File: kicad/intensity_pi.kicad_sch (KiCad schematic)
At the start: 67 parts, among them J1 Input A, J2 Input B / Setpoint, J3 Monitor, J4 Output, J7 select 1, SW1 SW_SPDT, SW2 SW_SPDT, SW3 SW_SPDT, SW5 EG6100-ND, U1 LM4040DBZ-5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

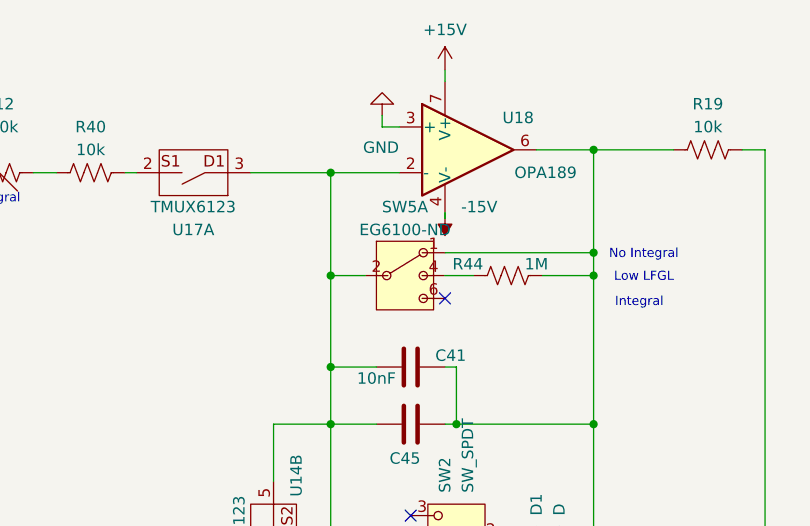
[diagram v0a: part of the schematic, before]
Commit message: Rearranged Edge Componenets, simpler board, wider but shorter depth
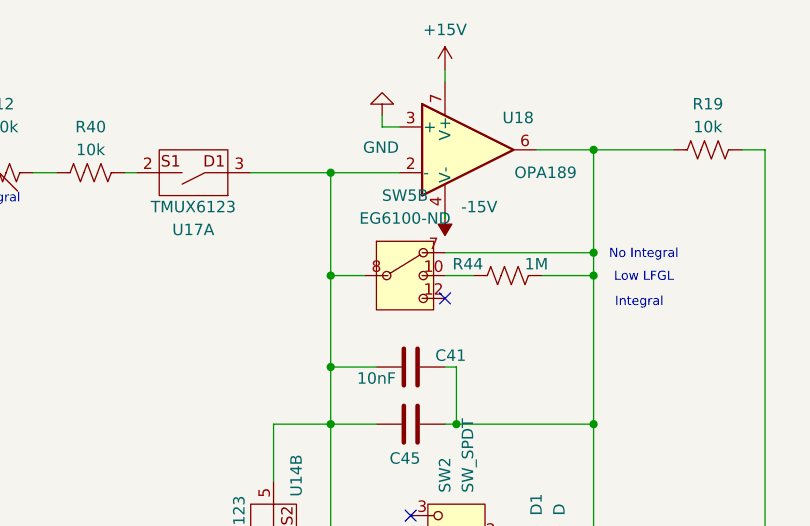
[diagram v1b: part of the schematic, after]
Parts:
- removed SW5: EG6100-ND, Custom_Footprints:Right Angle 3PDT Switch, symbol Custom_Symbols:DP3T_1
- added SW5: EG6100-ND, Custom_Footprints:Right Angle 3PDT Switch, symbol Custom_Symbols:DP3T_1
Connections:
- net at C41.1, C45.2, D1.2 (A)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: now also SW5.7
- net at C41.2, C45.1, SW2.1 (A)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: now also SW5.8
- net at R44.1: now also SW5.10
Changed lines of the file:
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@@
+	)
+	(symbol
+		(lib_id "Custom_Symbols:DP3T_1")
+		(at 179.07 41.91 0)
+		(unit 2)
+		(exclude_from_sim no)
+		(in_bom yes)
+		(on_board yes)
+		(dnp no)
+		(fields_autoplaced yes)
+		(property "Reference" "SW5"
+			(at 179.705 33.02 0)
+			(effects
+				(font
+					(size 1.27 1.27)
+				)
+			)
+		)
+		(property "Value" "EG6100-ND"
+			(at 179.705 35.56 0)
+			(effects
+				(font
+					(size 1.27 1.27)
+				)
+			)
+		)
+		(property "Footprint" "Custom_Footprints:Right Angle 3PDT Switch"
+			(at 179.07 41.91 0)
+			(effects
+				(font
+					(size 1.27 1.27)
+				)
+				(hide yes)
+			)
+		)
+		(property "Datasheet" ""
+			(at 179.07 41.91 0)
+			(effects
+				(font
+					(size 1.27 1.27)
+				)
+				(hide yes)
+			)
+		)
+		(property "Description" ""
+			(at 179.07 41.91 0)
+			(effects
+				(font
+					(size 1.27 1.27)
+				)
+				(hide yes)
+			)
+		)
+		(property "DIGIKEY" "EG6100-ND"
+			(at 179.07 41.91 0)
+			(effects
+				(font
+					(size 1.27 1.27)
+				)
+				(hide yes)
+			)
+		)
+		(property "PARTNO" "1004P6T1B4M7RE"
+			(at 179.07 41.91 0)
+			(effects
+				(font
+					(size 1.27 1.27)
+				)
+				(hide yes)
+			)
+		)
+		(property "MPN" ""
+			(at 179.07 41.91 0)
+			(effects
+				(font
+					(size 1.27 1.27)
+				)
+				(hide yes)
+			)
+		)
+		(pin "9"
+		)
+		(pin "10"
+		)
+		(pin "3"
+		)
+		(pin "5"
+		)
+		(pin "12"
+		)
+		(pin "8"
+		)
+		(pin "11"
+		)
+		(pin "7"
+		)
+		(pin "13"
+		)
+		(pin "6"
+		)
+		(pin "2"
+		)
+		(pin "4"
+		)
+		(pin "1"
+		)
+		(instances
+			(project "intensity_pi"
+				(path "/3a3d7bcb-6fa5-41ef-9ea1-6d4ab7c492fd"
+					(reference "SW5")
+					(unit 2)
+				)
+			)
+		)
 	)
 	(symbol
@@
 					(unit 1)
 				)
-			)
-		)
-	)
-	(symbol
-		(lib_id "Custom_Symbols:DP3T_1")
-		(at 179.07 41.91 0)
-		(unit 1)
-		(exclude_from_sim no)
-		(in_bom yes)
-		(on_board yes)
-		(dnp no)
-		(fields_autoplaced yes)
-		(property "Reference" "SW5"
-			(at 179.705 34.29 0)
-			(effects
-				(font
-					(size 1.27 1.27)
-				)
-			)
-		)
-		(property "Value" "EG6100-ND"
-			(at 179.705 36.83 0)
-			(effects
-				(font
-					(size 1.27 1.27)
-				)
-			)
-		)
-		(property "Footprint" "Custom_Footprints:Right Angle 3PDT Switch"
-			(at 179.07 41.91 0)
-			(effects
-				(font
-					(size 1.27 1.27)
-				)
-				(hide yes)
-			)
-		)
-		(property "Datasheet" ""
-			(at 179.07 41.91 0)
-			(effects
-				(font
-					(size 1.27 1.27)
-				)
-				(hide yes)
-			)
-		)
-		(property "Description" ""
-			(at 179.07 41.91 0)
-			(effects
-				(font
-					(size 1.27 1.27)
-				)
-				(hide yes)
-			)
-		)
-		(property "DIGIKEY" "EG6100-ND"
-			(at 179.07 41.91 0)
-			(effects
-				(font
-					(size 1.27 1.27)
-				)
-				(hide yes)
-			)
-		)
-		(property "PARTNO" "1004P6T1B4M7RE"
-			(at 179.07 41.91 0)
-			(effects
-				(font
-					(size 1.27 1.27)
-				)
-				(hide yes)
-			)
-		)
-		(property "MPN" ""
-			(at 179.07 41.91 0)
-			(effects
-				(font
-					(size 1.27 1.27)
-				)
-				(hide yes)
-			)
-		)
-		(pin "9"
-		)
-		(pin "10"
-		)
-		(pin "3"
-		)
-		(pin "5"
-		)
-		(pin "12"
-		)
-		(pin "8"
-		)
-		(pin "11"
-		)
-		(pin "7"
-		)
-		(pin "13"
-		)
-		(pin "6"
-		)
-		(pin "2"
-		)
-		(pin "4"
-		)
-		(pin "1"
-		)
-		(instances
-			(project "intensity_pi"
-				(path "/3a3d7bcb-6fa5-41ef-9ea1-6d4ab7c492fd"
-					(reference "SW5")
-					(unit 1)
-				)

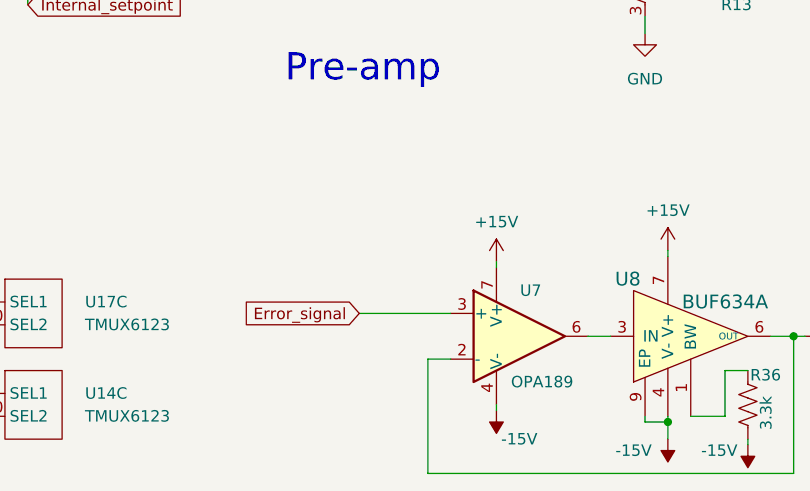
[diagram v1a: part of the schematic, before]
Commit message: Added 1k resistor to monitor, TODO: check BOM, reorg PI+LFGL, check power planes/return path, move A,B closer to PI, compress vertically
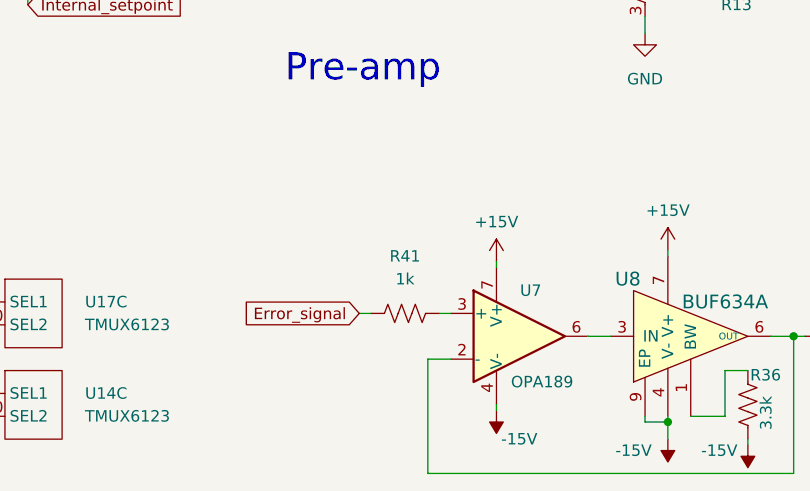
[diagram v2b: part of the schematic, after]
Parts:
- added R41: 1k, Resistor_SMD:R_0805_2012Metric, symbol Device:R_US
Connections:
- net Error_signal: now also R41.2; no longer U7.3 (+)
- new net: R41.1, U7.3 (+)
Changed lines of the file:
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@@
 	(wire
 		(pts
+			(xy 109.22 179.07) (xy 110.49 179.07)
+		)
+		(stroke
+			(width 0)
+			(type default)
+		)
+	)
+	(wire
+		(pts
 			(xy 241.935 114.3) (xy 262.89 114.3)
 		)
@@
 	(wire
 		(pts
-			(xy 109.22 179.07) (xy 119.38 179.07)
-		)
-		(stroke
-			(width 0)
-			(type default)
-		)
-	)
-	(wire
-		(pts
 			(xy 219.71 114.3) (xy 234.315 114.3)
 		)
@@
 	(wire
 		(pts
+			(xy 118.11 179.07) (xy 119.38 179.07)
+		)
+		(stroke
+			(width 0)
+			(type default)
+		)
+	)
+	(wire
+		(pts
 			(xy 25.4 67.31) (xy 25.4 69.85)
 		)
@@
 					(unit 1)
 				)
+			)
+		)
+	)
+	(symbol
+		(lib_id "Device:R_US")
+		(at 114.3 179.07 270)
+		(unit 1)
+		(exclude_from_sim no)
+		(in_bom yes)
+		(on_board yes)
+		(dnp no)
+		(fields_autoplaced yes)
+		(property "Reference" "R41"
+			(at 114.3 172.72 90)
+			(effects
+				(font
+					(size 1.27 1.27)
+				)
+			)
+		)
+		(property "Value" "1k"
+			(at 114.3 175.26 90)
+			(effects
+				(font
+					(size 1.27 1.27)
+				)
+			)
+		)
+		(property "Footprint" "Resistor_SMD:R_0805_2012Metric"
+			(at 114.046 180.086 90)
+			(effects
+				(font
+					(size 1.27 1.27)
+				)
+				(hide yes)
+			)
+		)
+		(property "Datasheet" "~"
+			(at 114.3 179.07 0)
+			(effects
+				(font
+					(size 1.27 1.27)
+				)
+				(hide yes)
+			)
+		)
+		(property "Description" ""
+			(at 114.3 179.07 0)
+			(effects
+				(font
+					(size 1.27 1.27)
+				)
+				(hide yes)
+			)
+		)
+		(property "DIGIKEY" ""
+			(at 114.3 179.07 0)
+			(effects
+				(font
+					(size 1.27 1.27)
+				)
+				(hide yes)
+			)
+		)
+		(property "MPN" ""
+			(at 114.3 179.07 0)
+			(effects
+				(font
+					(size 1.27 1.27)
+				)
+				(hide yes)
+			)
+		)
+		(pin "1"
+		)
+		(pin "2"
+		)
+		(instances
+			(project "intensity_pi"
+				(path "/3a3d7bcb-6fa5-41ef-9ea1-6d4ab7c492fd"
+					(reference "R41")
+					(unit 1)
+				)

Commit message: Minor Layout updates, replaced old component part no's, added part no's for rest of parts
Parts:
- C1, C10: DIGIKEY (none) -> 1276-6840-2-ND; PARTNO (none) -> CL21B104KCFNNNE
- C12: DIGIKEY (none) -> 399-C0805C101J5GACTUTR-ND; PARTNO (none) -> C0805C101J5GACTU
- C41: DIGIKEY (none) -> 399-C0805C103K5RACTUTR-ND; PARTNO (none) -> C0805C103K5RACTU
- R1, R10, R19, R2, R20, R22, R27, R3, R4, R40, R5, R6, R7, R8: PARTNO (none) -> RN73H2ATTD1002B25
- R12, RV8: DIGIKEY (none) -> 3590P-2-104L-ND; PARTNO (none) -> 3590P-2-104L
- R13: DIGIKEY (none) -> 118-CRT0805-BY-5001EASTR-ND; PARTNO (none) -> CRT0805-BY-5001EAS
- R14: DIGIKEY 2019-RN73H2ATTD1002B25CT-ND -> 3590S-2-103L-ND; PARTNO (none) -> 3590S-2-103L
- R15, R23: DIGIKEY (none) -> 541-CRCW080550R0FKTATR-ND; PARTNO (none) -> CRCW080550R0FKTA
- R16: DIGIKEY (none) -> P100KDATR-ND; PARTNO (none) -> ERA-6AEB104V
- R17, R21, R24, R26, R41, R9: DIGIKEY (none) -> 5831-2-2176327-5TR-ND; PARTNO (none) -> 2-2176327-5
- R33, R34: DIGIKEY 2019-RN73H2ATTD1002B25CT-ND -> (none)
- R35, R36: DIGIKEY 2019-RN73H2ATTD3301B25CT-ND -> 311-3.30KCRTR-ND; PARTNO (none) -> RC0805FR-073K3L
- R43, R46: DIGIKEY (none) -> A126334TR-ND; PARTNO (none) -> CRG0805F11K
- RV3: DIGIKEY (none) -> 3590S-2-502L-ND; PARTNO (none) -> 3590S-2-502L

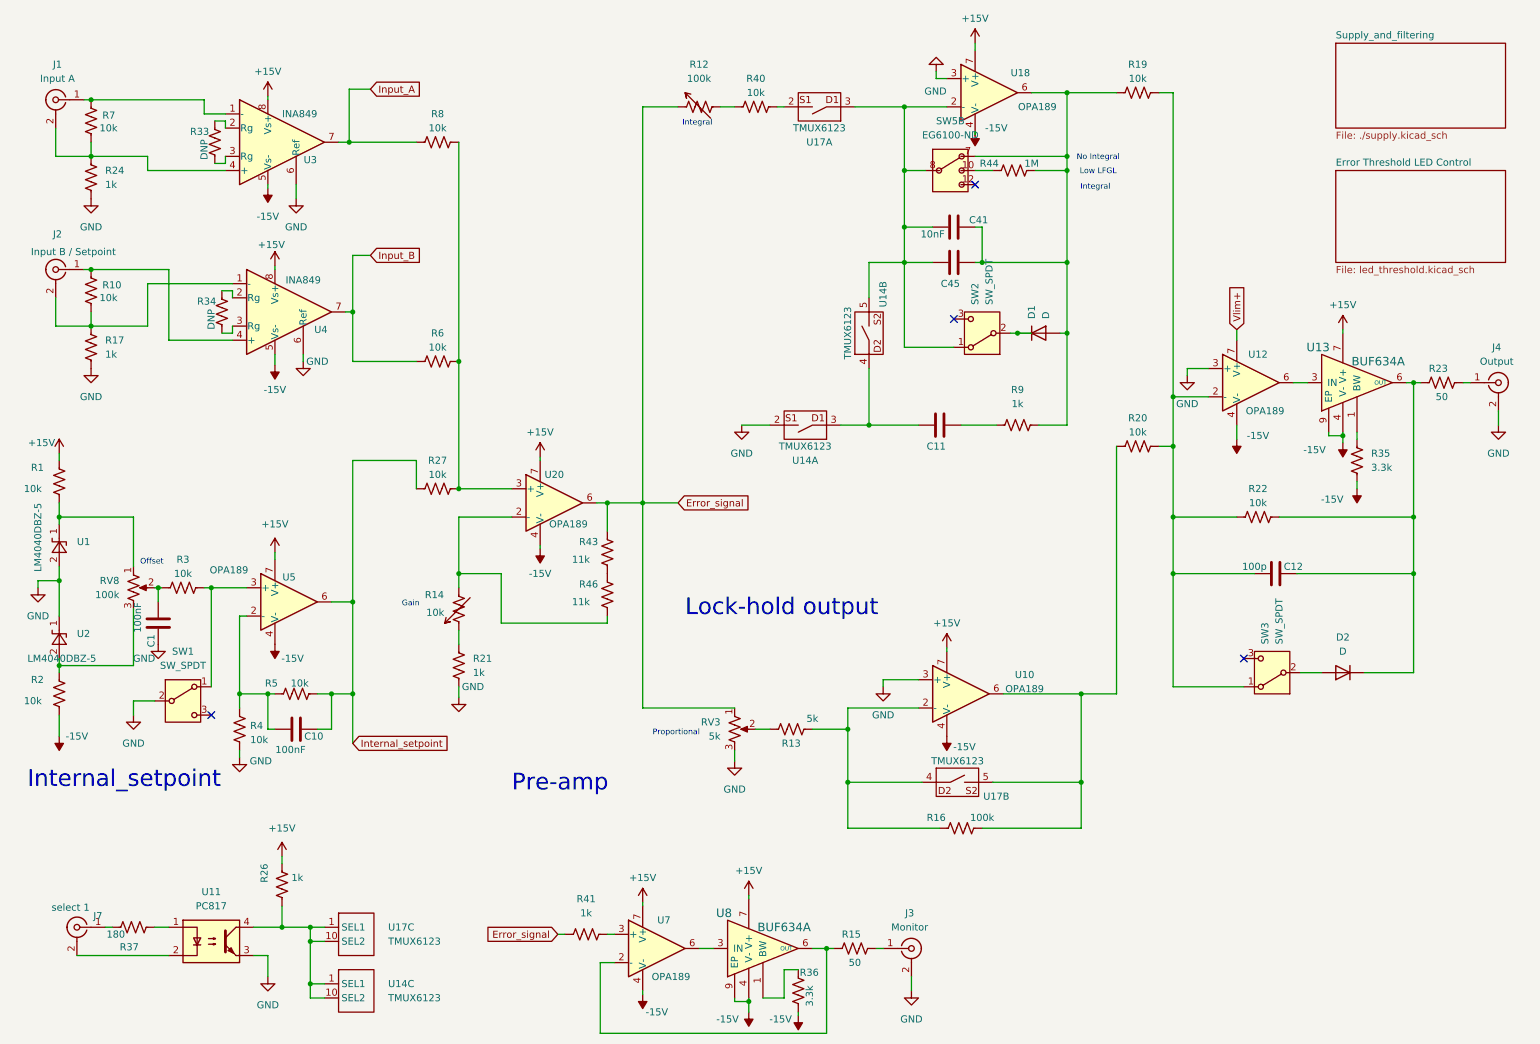
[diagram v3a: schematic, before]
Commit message: Revert change to Library Footprint for switch, update schematic to use resistance between pins 2,3 as starting at maximum, decreasing down on CW rotation
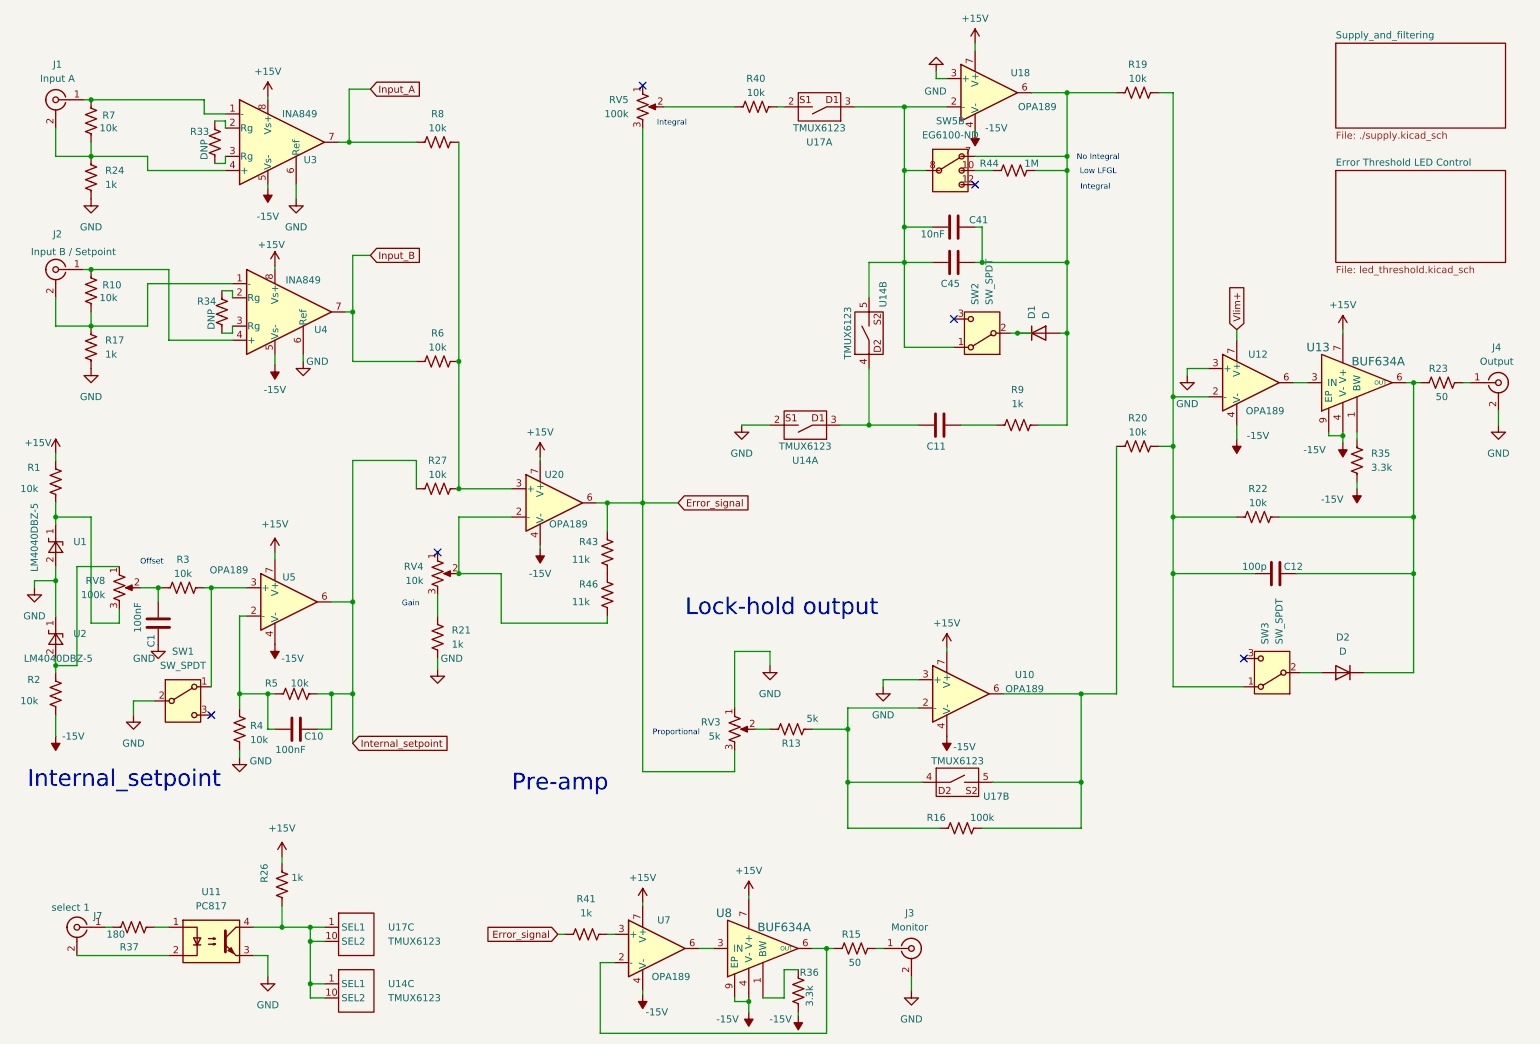
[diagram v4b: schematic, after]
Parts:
- removed R12: 100k, Custom_Footprints:Bourns Circular Pots, symbol Device:R_Variable_US
- removed R14: 10k, Custom_Footprints:Bourns Circular Pots, symbol Device:R_Variable_US
- added RV4: 10k, Custom_Footprints:Bourns Circular Pots, symbol Device:R_Potentiometer_US
- added RV5: 100k, Custom_Footprints:Bourns Circular Pots, symbol Device:R_Potentiometer_US
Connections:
- net Error_signal: now also RV3.3, RV5.3; no longer RV3.1
- net GND: now also RV3.1; no longer RV3.3
- net at R1.1, U1.1 (K): now also RV8.3; no longer RV8.1
- net at R2.2, U2.2 (A): now also RV8.1; no longer RV8.3
- net at R40.1: now also RV5.2
- net at R21.2: now also RV4.3
- net at R46.1, U20.2 (-): now also RV4.2
- no-connect marks 4 -> 6
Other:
- moved on the sheet: R1, R2, R21, RV8, U1, U2
